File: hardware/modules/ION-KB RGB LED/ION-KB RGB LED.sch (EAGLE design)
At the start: 3 parts

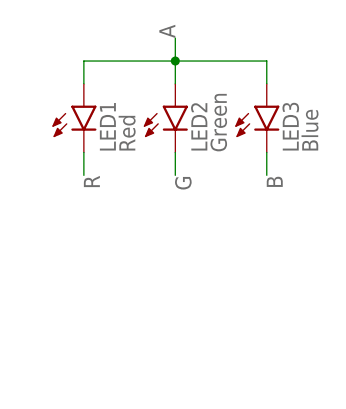
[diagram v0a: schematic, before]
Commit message: Switch to single RGB LED
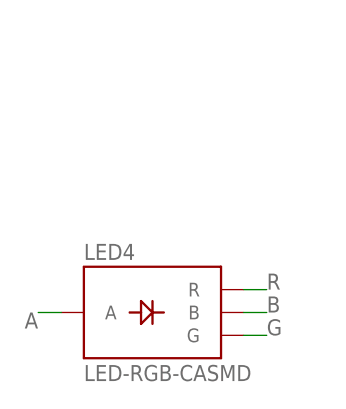
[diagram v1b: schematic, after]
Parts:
- removed LED1: Red, Jordi:LED0603
- removed LED2: Green, Jordi:LED0603
- removed LED3: Blue, Jordi:LED0603
- added LED4: LED-RGB-CASMD, Jordi:LED-RGB-CASMD
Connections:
- net A: now also LED4.A; no longer LED1.A, LED2.A, LED3.A
- net B: now also LED4.B; no longer LED3.C
- net G: now also LED4.G; no longer LED2.C
- net R: now also LED4.R; no longer LED1.C
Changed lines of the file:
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@@
 </classes>
 <parts>
-<part name="LED1" library="Jordi" deviceset="LED" device="0603" value="Red"/>
-<part name="LED2" library="Jordi" deviceset="LED" device="0603" value="Green"/>
-<part name="LED3" library="Jordi" deviceset="LED" device="0603" value="Blue"/>
+<part name="LED4" library="Jordi" deviceset="LED-RGB-CA" device="SMD"/>
 </parts>
 <sheets>
@@
 </plain>
 <instances>
-<instance part="LED1" gate="G$1" x="5.08" y="10.16" rot="R90"/>
-<instance part="LED2" gate="G$1" x="15.24" y="10.16" rot="R90"/>
-<instance part="LED3" gate="G$1" x="25.4" y="10.16" rot="R90"/>
+<instance part="LED4" gate="G$1" x="12.7" y="-12.7"/>
 </instances>
 <busses>
@@
 <net name="A" class="0">
 <segment>
-<pinref part="LED1" gate="G$1" pin="A"/>
-<wire x1="5.08" y1="15.24" x2="5.08" y2="12.7" width="0.1524" layer="91"/>
-<pinref part="LED2" gate="G$1" pin="A"/>
-<wire x1="5.08" y1="15.24" x2="15.24" y2="15.24" width="0.1524" layer="91"/>
-<wire x1="15.24" y1="15.24" x2="15.24" y2="12.7" width="0.1524" layer="91"/>
-<pinref part="LED3" gate="G$1" pin="A"/>
-<wire x1="15.24" y1="15.24" x2="25.4" y2="15.24" width="0.1524" layer="91"/>
-<wire x1="25.4" y1="15.24" x2="25.4" y2="12.7" width="0.1524" layer="91"/>
-<junction x="15.24" y="15.24"/>
-<wire x1="15.24" y1="15.24" x2="15.24" y2="17.78" width="0.1524" layer="91"/>
-<label x="15.24" y="17.78" size="1.778" layer="95" rot="R90"/>
+<pinref part="LED4" gate="G$1" pin="A"/>
+<wire x1="2.54" y1="-12.7" x2="0" y2="-12.7" width="0.1524" layer="91"/>
+<label x="0" y="-12.7" size="1.778" layer="95" rot="R180"/>
 </segment>
 </net>
 <net name="R" class="0">
 <segment>
-<pinref part="LED1" gate="G$1" pin="C"/>
-<wire x1="5.08" y1="5.08" x2="5.08" y2="2.54" width="0.1524" layer="91"/>
-<label x="5.08" y="2.54" size="1.778" layer="95" rot="R270"/>
+<pinref part="LED4" gate="G$1" pin="R"/>
+<wire x1="22.86" y1="-10.16" x2="25.4" y2="-10.16" width="0.1524" layer="91"/>
+<label x="25.4" y="-10.16" size="1.778" layer="95"/>
 </segment>
 </net>
 <net name="G" class="0">
 <segment>
-<pinref part="LED2" gate="G$1" pin="C"/>
-<wire x1="15.24" y1="5.08" x2="15.24" y2="2.54" width="0.1524" layer="91"/>
-<label x="15.24" y="2.54" size="1.778" layer="95" rot="R270"/>
+<pinref part="LED4" gate="G$1" pin="G"/>
+<wire x1="22.86" y1="-15.24" x2="25.4" y2="-15.24" width="0.1524" layer="91"/>
+<label x="25.4" y="-15.24" size="1.778" layer="95"/>
 </segment>
 </net>
 <net name="B" class="0">
 <segment>
-<pinref part="LED3" gate="G$1" pin="C"/>
-<wire x1="25.4" y1="5.08" x2="25.4" y2="2.54" width="0.1524" layer="91"/>
-<label x="25.4" y="2.54" size="1.778" layer="95" rot="R270"/>
+<pinref part="LED4" gate="G$1" pin="B"/>
+<wire x1="22.86" y1="-12.7" x2="25.4" y2="-12.7" width="0.1524" layer="91"/>
+<label x="25.4" y="-12.7" size="1.778" layer="95"/>
 </segment>
 </net>
